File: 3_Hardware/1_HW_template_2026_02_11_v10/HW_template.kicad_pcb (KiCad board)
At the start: 4 copper layers, 63.5 x 118.1 mm, 86 parts, among them J1 AudioJack3, P1 type="R" model="Conn_01x32_Fe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, P2 type="R" model="Conn_01x32_Fe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, U1 MCP6002-xSN, U2 MCP6002-xSN, U3 MCP6002-xSN, U4 LD1117S33TR_SOT223, U5 AD8232ACPZ-R7, Y1 Radar K-LC5-RFB-00C, Y2 OpenLog

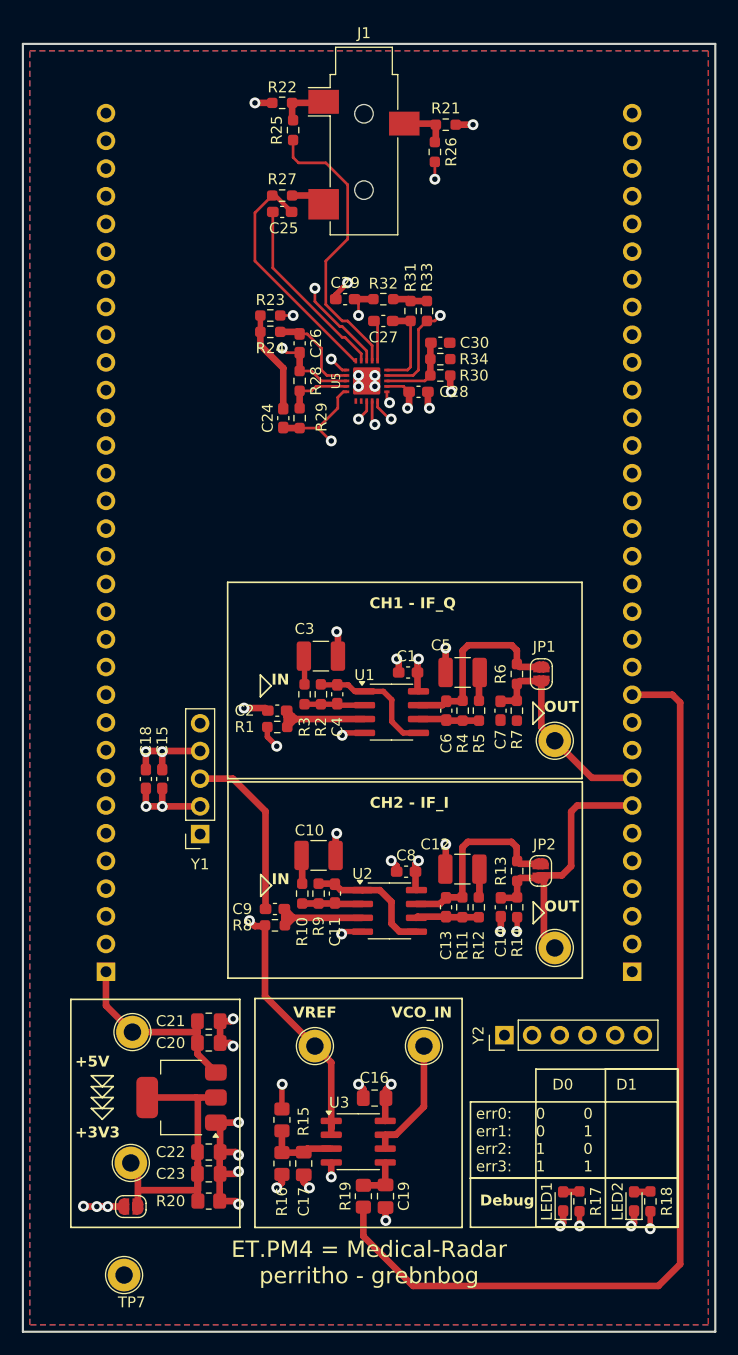
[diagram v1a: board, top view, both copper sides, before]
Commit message: fixed footprints
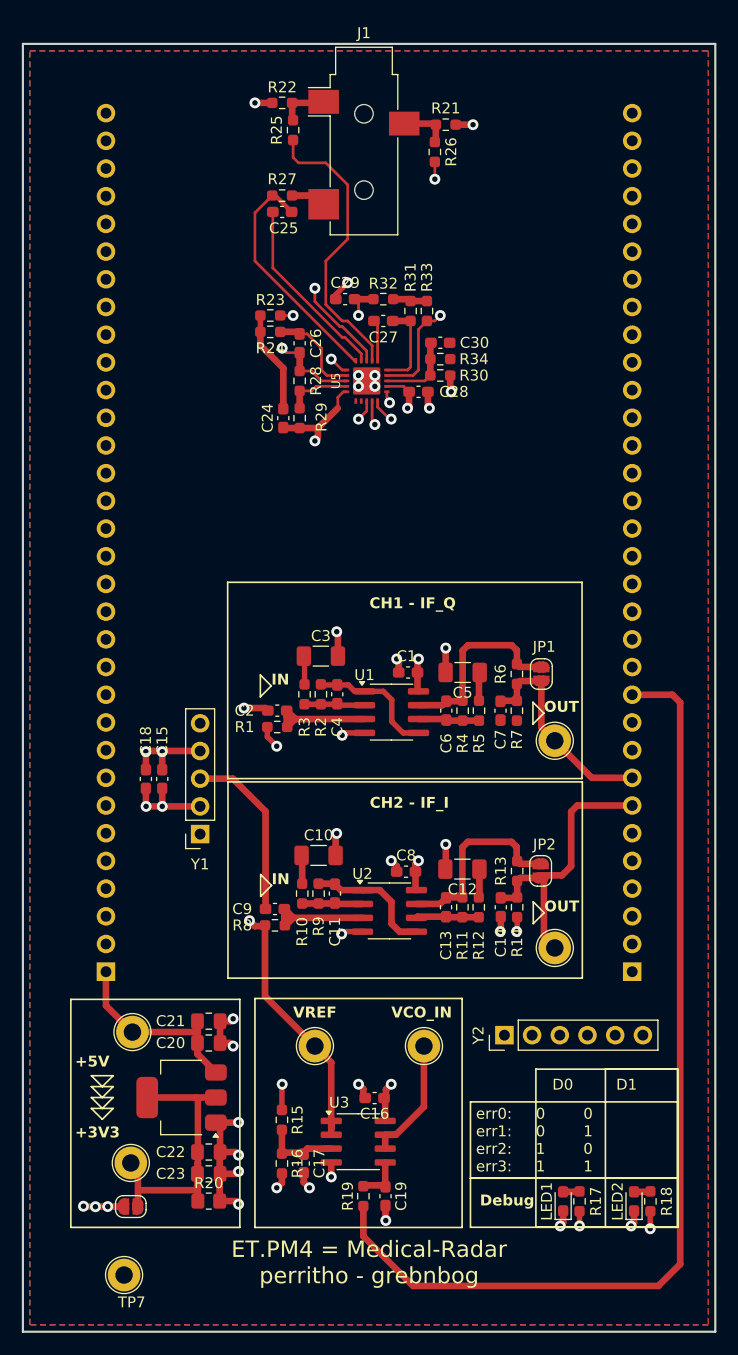
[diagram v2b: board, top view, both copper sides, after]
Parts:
- C10, C12, C3, C5: footprint Capacitor_SMD:C_1210_3225Metric_Pad1.33x2.70mm_HandSolder -> Capacitor_SMD:C_1206_3216Metric_Pad1.33x1.80mm_HandSolder
- C16, C17, C19: footprint Capacitor_SMD:C_0805_2012Metric_Pad1.18x1.45mm_HandSolder -> Capacitor_SMD:C_0603_1608Metric_Pad1.08x0.95mm_HandSolder
- C22: value 10uF -> 10u
- R15, R16, R19: footprint Resistor_SMD:R_0805_2012Metric_Pad1.20x1.40mm_HandSolder -> Resistor_SMD:R_0603_1608Metric_Pad0.98x0.95mm_HandSolder
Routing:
- net PF6: track 77.3 -> 67.8 mm

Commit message: designed pcb
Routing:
- net PA5: track 90.6 -> 74.5 mm, vias 0 -> 1
- net PE3: track 103.2 -> 98.7 mm
- net PE5: track 91.2 -> 86.9 mm
- net 3V3_INT: track 36.6 -> 36.2 mm, vias 15 -> 14
- net GND: vias 32 -> 170
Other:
- board text added: "J1"
- board text added: "ZHAW"

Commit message: finalized pcb
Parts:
- Y2: footprint Connector_PinHeader_2.54mm:PinHeader_1x06_P2.54mm_Vertical -> Connector_PinSocket_2.54mm:PinSocket_1x06_P2.54mm_Vertical
- renumbered TP7 to GND
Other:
- board text removed: "J1"
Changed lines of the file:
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@@
 		)
 	)
-	(footprint "Connector_PinHeader_2.54mm:PinHeader_1x06_P2.54mm_Vertical"
+	(footprint "Connector_PinSocket_2.54mm:PinSocket_1x06_P2.54mm_Vertical"
 		(layer "F.Cu")
 		(at 89.88 112.5 90)
-		(descr "Through hole straight pin header, 1x06, 2.54mm pitch, single row")
-		(tags "Through hole pin header THT 1x06 2.54mm single row")
+		(descr "Through hole straight socket strip, 1x06, 2.54mm pitch, single row (from Kicad 4.0.7), script generated")
+		(tags "Through hole socket strip THT 1x06 2.54mm single row")
 		(property "Reference" "Y2"
-			(at 0 -2.38 90)
+			(at 0 -2.77 90)
 			(layer "F.SilkS")
 			(effects
@@
 		)
 		(property "Value" "OpenLog"
-			(at 0 15.08 90)
+			(at 0 15.47 90)
 			(layer "F.Fab")
-			(hide yes)
 			(effects
 				(font
@@
 		(attr through_hole)
 		(fp_line
-			(start -1.38 -1.38)
-			(end 0 -1.38)
+			(start 1.33 -1.33)
+			(end 1.33 0)
 			(stroke
 				(width 0.12)
@@
 		)
 		(fp_line
-			(start -1.38 0)
-			(end -1.38 -1.38)
+			(start 0 -1.33)
+			(end 1.33 -1.33)
 			(stroke
 				(width 0.12)
@@
 		)
 		(fp_line
-			(start 1.38 1.27)
-			(end 1.38 14.08)
+			(start 1.33 1.27)
+			(end 1.33 14.03)
 			(stroke
 				(width 0.12)
@@
 		)
 		(fp_line
-			(start -1.38 1.27)
-			(end 1.38 1.27)
+			(start -1.33 1.27)
+			(end 1.33 1.27)
 			(stroke
 				(width 0.12)
@@
 		)
 		(fp_line
-			(start -1.38 1.27)
-			(end -1.38 14.08)
+			(start -1.33 1.27)
+			(end -1.33 14.03)
 			(stroke
 				(width 0.12)
@@
 		)
 		(fp_line
-			(start -1.38 14.08)
-			(end 1.38 14.08)
+			(start -1.33 14.03)
+			(end 1.33 14.03)
 			(stroke
 				(width 0.12)
@@
 		)
 		(fp_line
-			(start 1.77 -1.77)
-			(end -1.77 -1.77)
+			(start 1.75 -1.8)
+			(end 1.75 14.45)
 			(stroke
 				(width 0.05)
@@
 		)
 		(fp_line
-			(start -1.77 -1.77)
-			(end -1.77 14.47)
+			(start -1.8 -1.8)
+			(end 1.75 -1.8)
 			(stroke
 				(width 0.05)
@@
 		)
 		(fp_line
-			(start 1.77 14.47)
-			(end 1.77 -1.77)
+			(start 1.75 14.45)
+			(end -1.8 14.45)
 			(stroke
 				(width 0.05)
@@
 		)
 		(fp_line
-			(start -1.77 14.47)
-			(end 1.77 14.47)
+			(start -1.8 14.45)
+			(end -1.8 -1.8)
 			(stroke
 				(width 0.05)
@@
 		)
 		(fp_line
-			(start 1.27 -1.27)
-			(end 1.27 13.97)
+			(start 0.635 -1.27)
+			(end 1.27 -0.635)
 			(stroke
 				(width 0.1)
@@
 		)
 		(fp_line
-			(start -0.635 -1.27)
-			(end 1.27 -1.27)
+			(start -1.27 -1.27)
+			(end 0.635 -1.27)
 			(stroke
 				(width 0.1)
@@
 		)
 		(fp_line
-			(start -1.27 -0.635)
-			(end -0.635 -1.27)
+			(start 1.27 -0.635)
+			(end 1.27 13.97)
 			(stroke
 				(width 0.1)
@@
 		(fp_line
 			(start -1.27 13.97)
-			(end -1.27 -0.635)
+			(end -1.27 -1.27)
 			(stroke
 				(width 0.1)
@@
 		)
 		(fp_text user "${REFERENCE}"
-			(at 0 6.35 0)
+			(at 0 6.35 180)
 			(layer "F.Fab")
 			(effects
@@
 			(net 54 "unconnected-(Y2-GRN-Pad1)")
 			(pinfunction "GRN")
-			(pintype "input")
+			(pintype "input+no_connect")
 		)
 		(pad "2" thru_hole circle
@@
 			(net 55 "unconnected-(Y2-TXO-Pad3)")
 			(pinfunction "TXO")
-			(pintype "output")
+			(pintype "output+no_connect")
 		)
 		(pad "4" thru_hole circle
@@
 		)
 		(embedded_fonts no)
-		(model "${KICAD9_3DMODEL_DIR}/Connector_PinHeader_2.54mm.3dshapes/PinHeader_1x06_P2.54mm_Vertical.step"
+		(model "${KICAD9_3DMODEL_DIR}/Connector_PinSocket_2.54mm.3dshapes/PinSocket_1x06_P2.54mm_Vertical.step"
 			(offset
 				(xyz 0 0 0)
@@
 		)
 		(embedded_fonts no)
-		(model "/home/thomas/Documents/git/PM4/3_Hardware/8_Component_libs/AD8232/AD8232.step"
+		(model "${KIPRJMOD}/Component_libs/AD8232/AD8232.step"
 			(offset
 				(xyz 0 0 0)
@@
 		(descr "wire loop with bead as test point, loop diameter2.6mm, hole diameter 1.6mm")
 		(tags "test point wire loop bead")
-		(property "Reference" "TP7"
-			(at 3.8 0.3 0)
+		(property "Reference" "GND"
+			(at -4.2 -0.1 0)
 			(layer "F.SilkS")
 			(effects
@@
 			)
 		)
-	)
-	(gr_text "J1"
-		(at 76.8 135.4 0)
-		(layer "F.SilkS")
-		(effects
-			(font
-				(size 1 1)
-				(thickness 0.15)
-			)
-		)

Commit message: minor pcb improvements + bom
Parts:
- P1, P2: value type="R" model="Conn_01x32_Female" lib="" -> Conn_01x32_Female
- TP1, TP2, TP4: value Channel1 -> ~
- renumbered GND to TP7

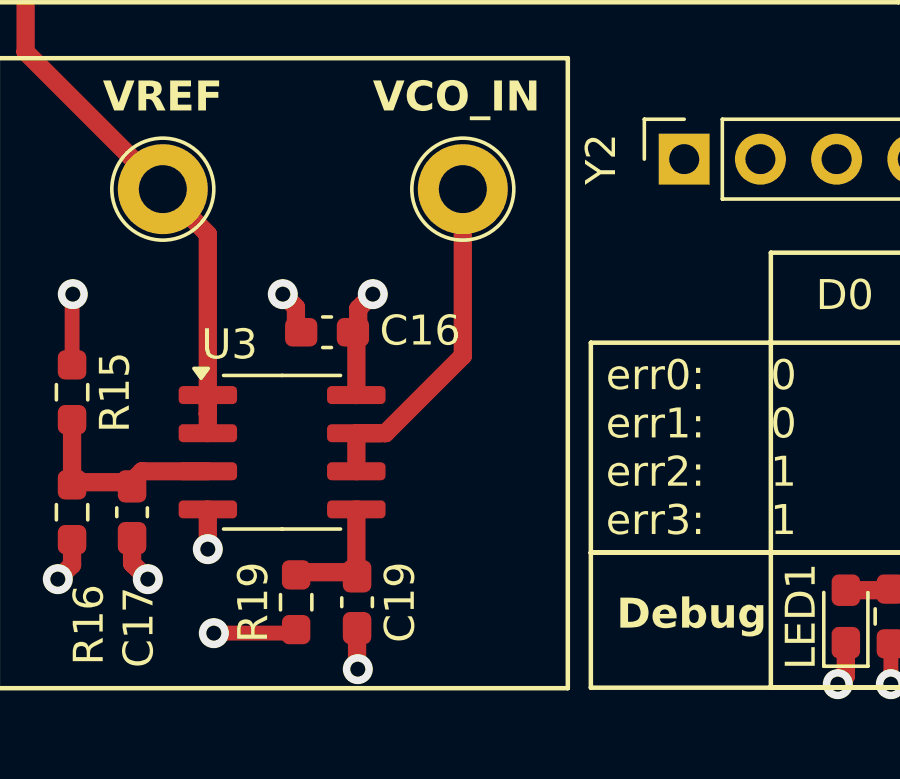
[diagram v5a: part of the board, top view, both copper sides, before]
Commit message: added amplification to VCO
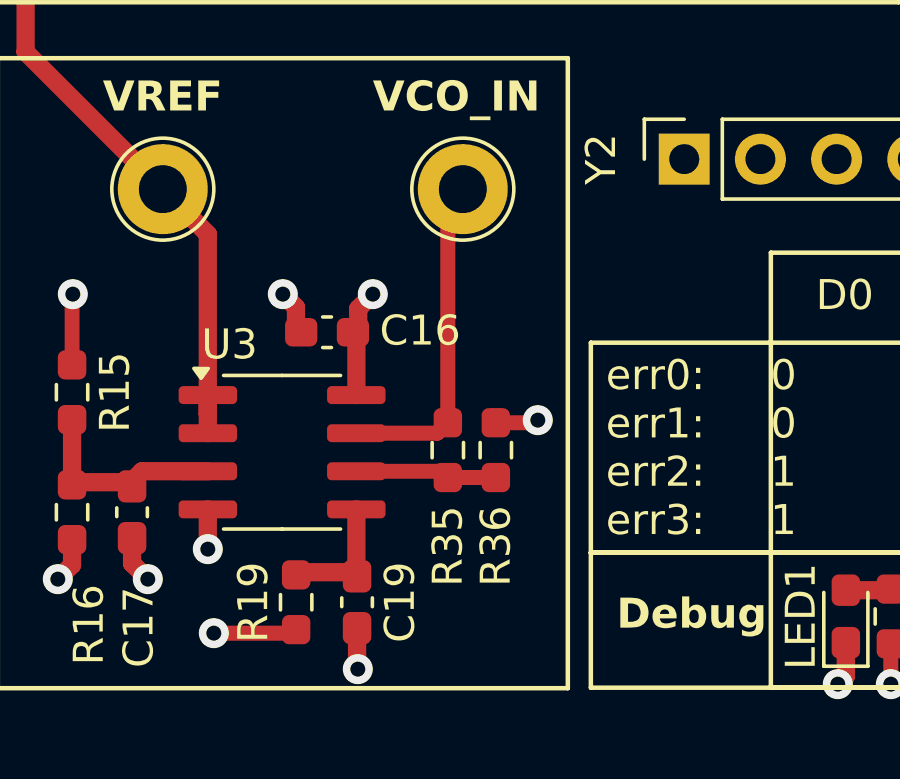
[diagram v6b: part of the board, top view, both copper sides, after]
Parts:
- added R35: 11k, Resistor_SMD:R_0603_1608Metric_Pad0.98x0.95mm_HandSolder, F.Cu at (82.0, 122.2)
- added R36: 10k, Resistor_SMD:R_0603_1608Metric_Pad0.98x0.95mm_HandSolder, F.Cu at (83.6, 122.2)
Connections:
- U3 pad 6: /Analog/VCO_in -> Net-(U3B--)
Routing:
- net Net-(U3B--): track 0.00 -> 4.74 mm
- net GND: track 64.2 -> 65.7 mm, vias 170 -> 171
